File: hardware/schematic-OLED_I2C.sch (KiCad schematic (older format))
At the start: 12 parts

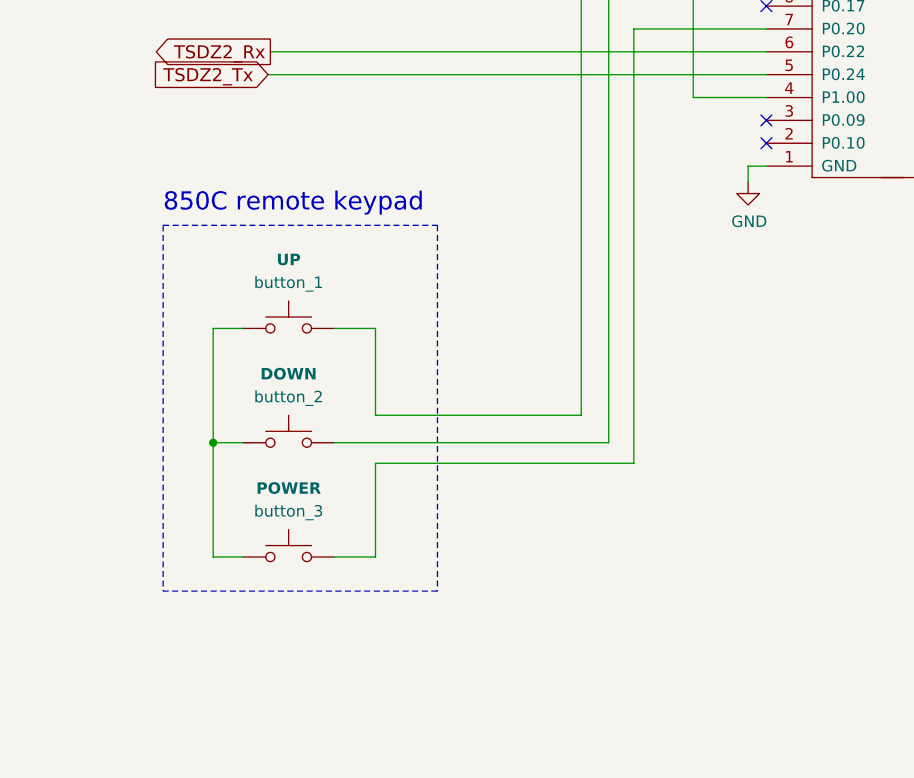
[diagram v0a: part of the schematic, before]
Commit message: Updated schematic on missing GND for buttons
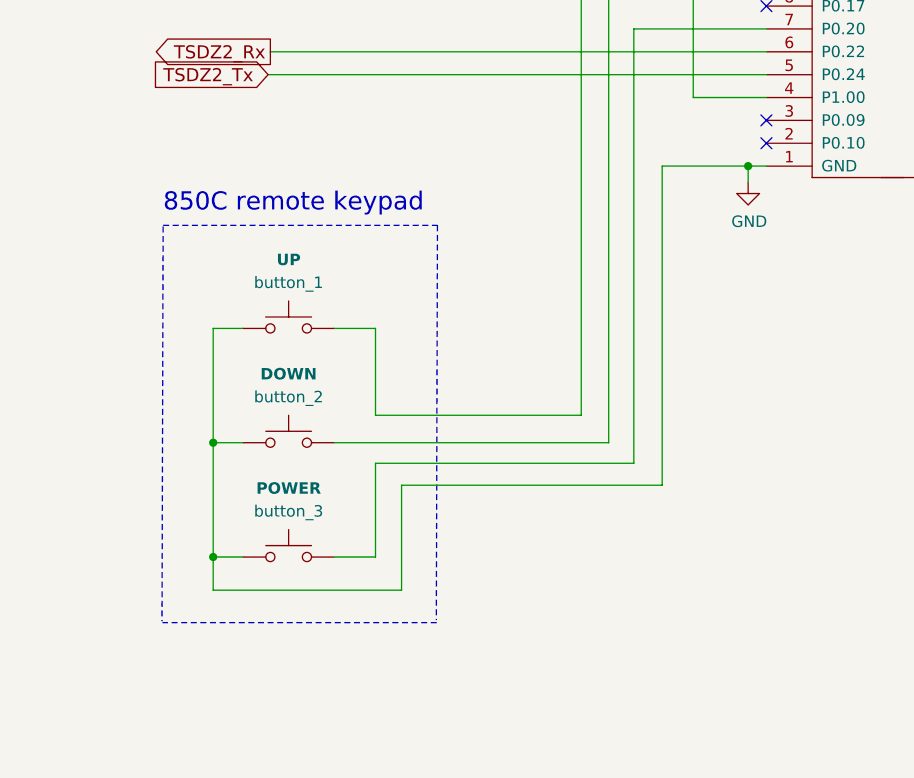
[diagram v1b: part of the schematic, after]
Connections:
- net GND: now also button_1.1, button_2.1, button_3.1
- net at U?.2 (VDD_out): now also Brd?.2 (VCC)
- net at U?.4 (P1.00): now also U?.1
- net at U?.8 (P1.13): now also Brd?.4 (SDA)
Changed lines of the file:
@@
 	7737 5623 8937 5623
 Wire Notes Line
-	8937 5623 8937 7223
-Wire Notes Line
-	8937 7223 7737 7223
+	8937 5623 8932 7350
+Wire Notes Line
+	8934 7361 7734 7361
 Text Notes 7737 5573 0    79   ~ 0
 850C remote keypad
@@
 Text GLabel 5214 7529 2    50   Input ~ 0
 TSDZ2_5V
-Wire Notes Line
-	7737 5623 7737 7223
 $Comp
 L Wired_remote:Switch_SW_Push button_3
@@
 	7956 6574 8086 6574
 Wire Wire Line
-	7956 6574 7956 7074
-Wire Wire Line
 	7956 7074 8086 7074
 Connection ~ 7956 6574
@@
 Wire Wire Line
 	4099 7629 5214 7629
+Wire Wire Line
+	10296 5364 9920 5364
+Wire Wire Line
+	9920 5364 9920 6760
+Wire Wire Line
+	9920 6760 8780 6760
+Connection ~ 10296 5364
+Wire Wire Line
+	7956 7219 8780 7219
+Wire Wire Line
+	7956 6574 7956 7074
+Wire Wire Line
+	8780 6760 8780 7219
+Connection ~ 7956 7074
+Wire Wire Line
+	7956 7074 7956 7219
+Wire Notes Line
+	7737 5628 7732 7355
 $EndSCHEMATC
